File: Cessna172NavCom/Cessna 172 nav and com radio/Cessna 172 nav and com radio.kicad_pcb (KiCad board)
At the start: 2 copper layers, 33 parts, among them J1 Board connector, U1 MAX7219 COM standby, U2 MAX7219 COM standby, U3 MAX7219 COM standby, U4 MAX7219 COM standby

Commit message: 3D model for LED
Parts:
- added C5: 0.1uf, Capacitor_THT:C_Disc_D3.0mm_W2.0mm_P2.50mm, F.Cu at (189.8, 95.3)
- added C6: 0.1uf, Capacitor_THT:C_Disc_D3.0mm_W2.0mm_P2.50mm, F.Cu at (213.0, 52.6)
- added J1: Conn_02x08_Counter_Clockwise, Connector_PinHeader_2.54mm:PinHeader_1x16_P2.54mm_Vertical, F.Cu at (190.5, 53.1)
- added R5: 10k, Resistor_SMD:R_0805_2012Metric_Pad1.15x1.40mm_HandSolder, F.Cu at (195.2, 67.5)
- added R6: 10k, Resistor_SMD:R_0805_2012Metric_Pad1.15x1.40mm_HandSolder, F.Cu at (200.0, 67.5)
- added R7: 10k, Resistor_SMD:R_0805_2012Metric_Pad1.15x1.40mm_HandSolder, F.Cu at (204.7, 67.5)
- added R8: 10k, Resistor_SMD:R_0805_2012Metric_Pad1.15x1.40mm_HandSolder, F.Cu at (209.5, 67.5)
- added SW1: Tuning encoder, Rotary_Encoder:RotaryEncoder_Alps_EC11E-Switch_Vertical_H20mm, F.Cu at (194.9, 55.9)
- LED1, LED10, LED11, LED12, LED13, LED14, LED15, LED16, LED17, LED18, LED19, LED2, LED20, LED3, LED4, LED5, LED6, LED7, LED8, LED9: footprint Display_7Segment:KCSC02-105 -> Cessna 172 nav and com radio:KYX-5101AS
- U1, U2, U3, U4: footprint Package_DIP:DIP-24_W7.62mm -> Package_SO:SSOP-24_3.9x8.7mm_P0.635mm
- moved LED6 37.5 mm to (55.9, 86.4)
- moved LED7 22.8 mm to (94.0, 86.4)
- moved LED8 22.2 mm to (68.6, 86.4)
- moved LED10 14.6 mm to (106.7, 86.4)
- moved LED9 7.07 mm to (81.3, 86.4)

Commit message: 3d model updates
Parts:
- R1, R2, U1, U2: moved to B.Cu
- moved R2 52.3 mm to (59.7, 48.3)
- moved R1 51.9 mm to (58.4, 26.7)
- moved LED3 41.7 mm to (45.7, 26.7)
- moved LED10 39.4 mm to (96.5, 48.3)
- moved LED7 39.4 mm to (83.8, 48.3)
- moved LED6 39.4 mm to (45.7, 48.3)
- moved LED8 39.4 mm to (58.4, 48.3)
- moved LED9 39.4 mm to (71.1, 48.3)
- moved LED4 29.6 mm to (71.1, 26.7)
- moved LED5 27.9 mm to (58.4, 26.7)
- moved LED2 17.8 mm to (83.8, 26.7)
- moved U2 14.2 mm to (71.1, 48.3), turned to 270 degrees
- moved LED1 10.0 mm to (96.5, 26.7)
- moved U1 1.88 mm to (71.1, 26.7), turned to 270 degrees

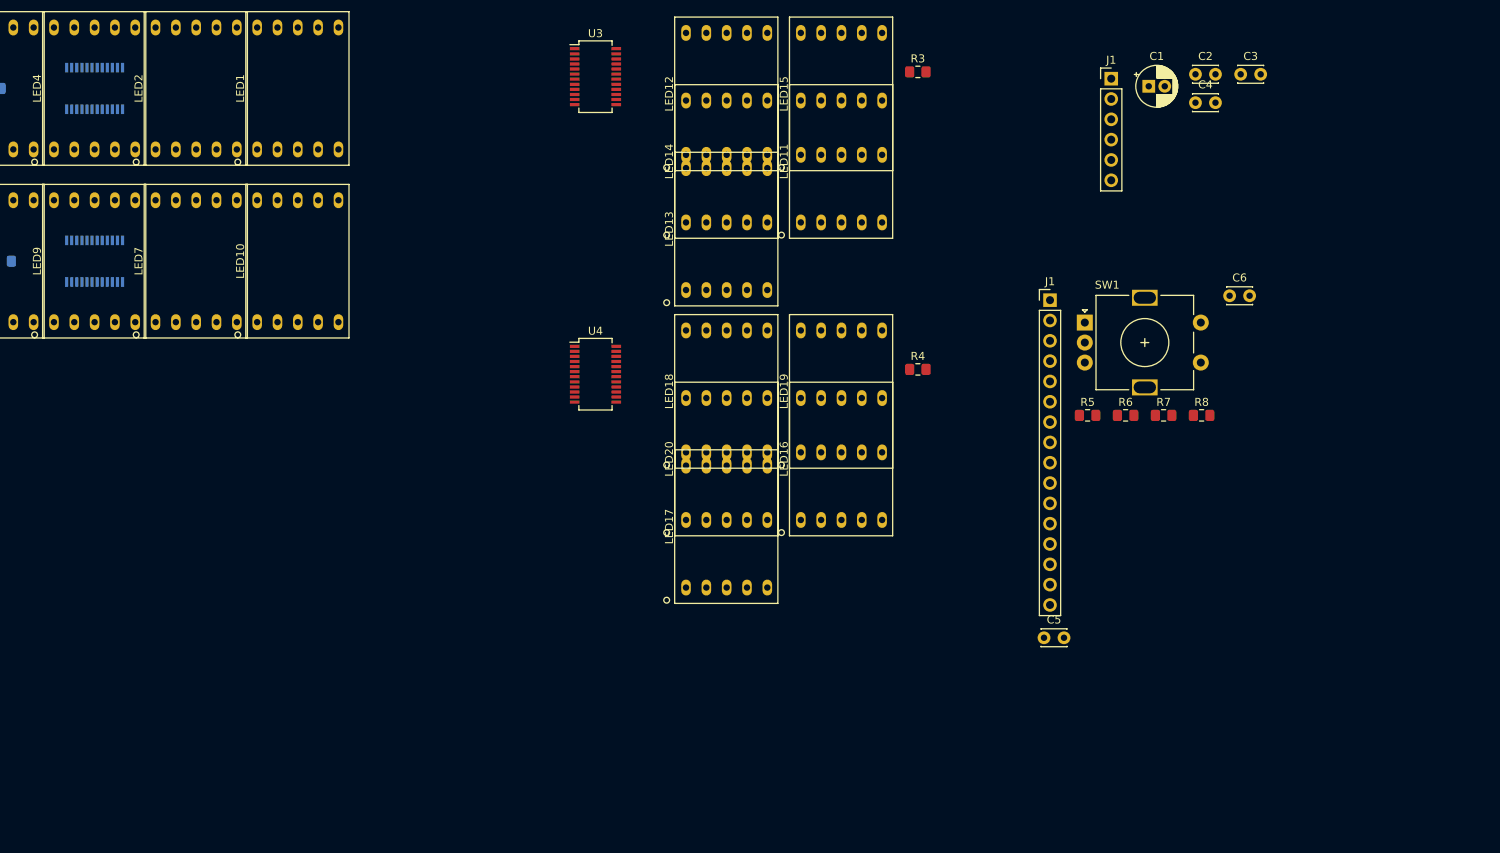
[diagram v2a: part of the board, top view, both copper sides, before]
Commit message: Updated schematic to include remaining items.
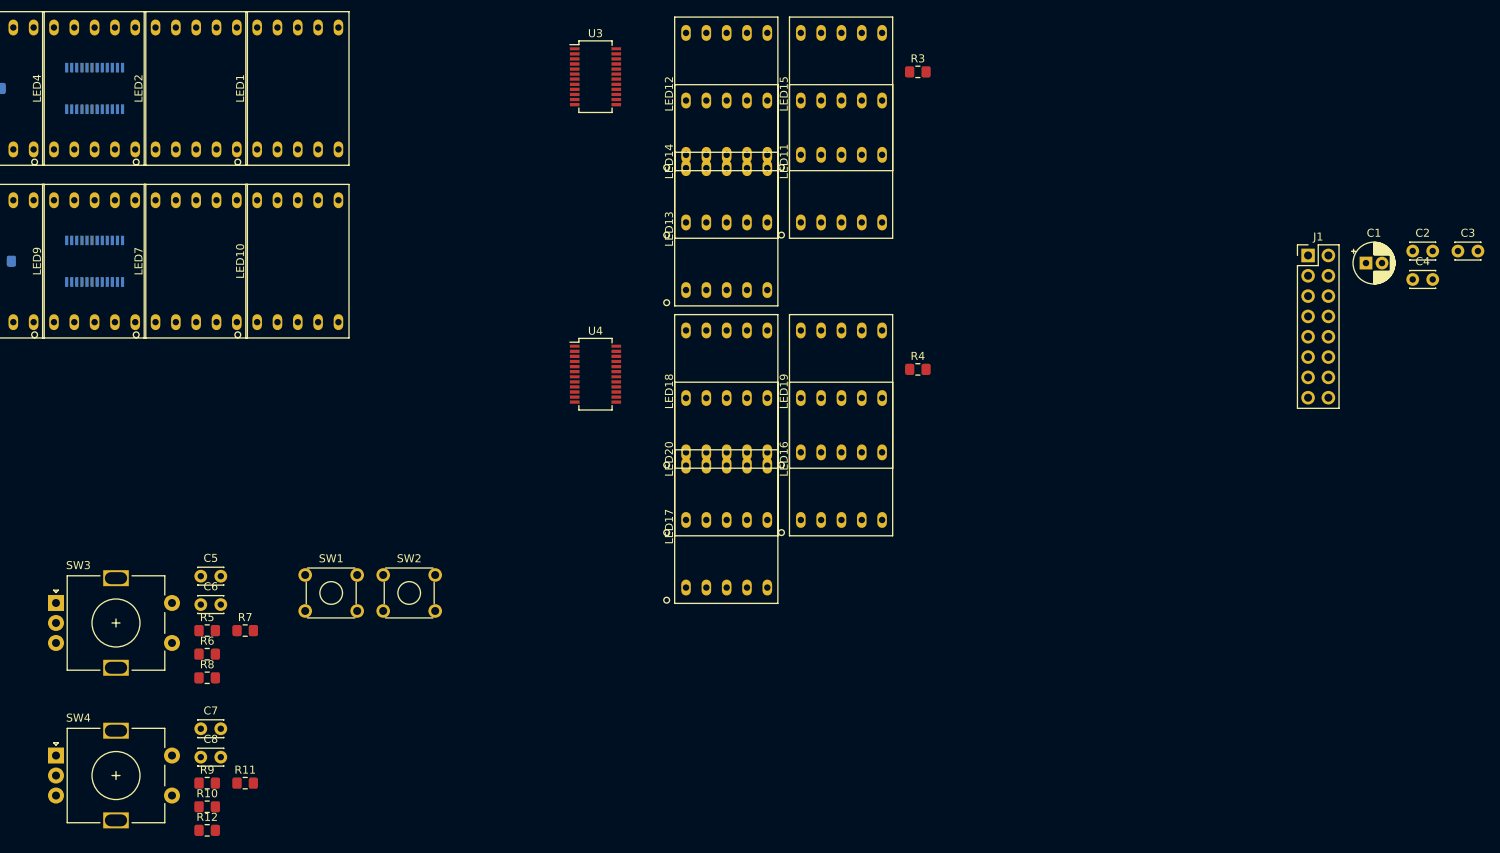
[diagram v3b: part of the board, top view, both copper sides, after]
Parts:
- removed the J1 at (198.2, 25.4)
- removed the J1 at (190.5, 53.1)
- added C7: 0.1uf, Capacitor_THT:C_Disc_D3.0mm_W2.0mm_P2.50mm, F.Cu at (84.4, 106.7)
- added C8: 0.1uf, Capacitor_THT:C_Disc_D3.0mm_W2.0mm_P2.50mm, F.Cu at (84.4, 110.3)
- added J1: Conn_02x08_Counter_Clockwise, Connector_PinHeader_2.54mm:PinHeader_2x08_P2.54mm_Vertical, F.Cu at (222.8, 47.5)
- added R10: 10k, Resistor_SMD:R_0805_2012Metric_Pad1.15x1.40mm_HandSolder, F.Cu at (85.2, 116.5)
- added R11: 10k, Resistor_SMD:R_0805_2012Metric_Pad1.15x1.40mm_HandSolder, F.Cu at (89.9, 113.5)
- added R12: 10k, Resistor_SMD:R_0805_2012Metric_Pad1.15x1.40mm_HandSolder, F.Cu at (85.2, 119.4)
- added R9: 10k, Resistor_SMD:R_0805_2012Metric_Pad1.15x1.40mm_HandSolder, F.Cu at (85.2, 113.5)
- added SW2: NAV transfer switch, Button_Switch_THT:SW_TH_Tactile_Omron_B3F-10xx, F.Cu at (107.2, 87.5)
- added SW3: Tuning encoder, Rotary_Encoder:RotaryEncoder_Alps_EC11E-Switch_Vertical_H20mm, F.Cu at (66.3, 91.0)
- added SW4: Tuning encoder, Rotary_Encoder:RotaryEncoder_Alps_EC11E-Switch_Vertical_H20mm, F.Cu at (66.3, 110.1)
- SW1: value Tuning encoder -> COMM transfer switch; footprint Rotary_Encoder:RotaryEncoder_Alps_EC11E-Switch_Vertical_H20mm -> Button_Switch_THT:SW_TH_Tactile_Omron_B3F-10xx
- moved C6 134.3 mm to (84.4, 91.2)
- moved R8 128.6 mm to (85.2, 100.3)
- moved R6 118.6 mm to (85.2, 97.4)
- moved R7 117.9 mm to (89.9, 94.4)
- moved R5 113.3 mm to (85.2, 94.4)
- moved C5 105.7 mm to (84.4, 87.6)
- moved SW1 102.4 mm to (97.4, 87.5)
- moved C1 35.0 mm to (230.0, 48.5)
- moved C3 35.0 mm to (241.5, 47.0)
- moved C2 35.0 mm to (235.9, 47.0)
- moved C4 35.0 mm to (235.9, 50.5)
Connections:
- R5 pad 1: R_RIGHT -> Net-(C5-Pad2)
- R5 pad 2: Net-(C5-Pad2) -> +5V
- R6 pad 1: Net-(C5-Pad2) -> Net-(C6-Pad1)
- R7 pad 1: Net-(C6-Pad1) -> COMM_RIGHT
- R7 pad 2: +5V -> Net-(C5-Pad2)
- R8 pad 2: R_LEFT -> COMM_LEFT

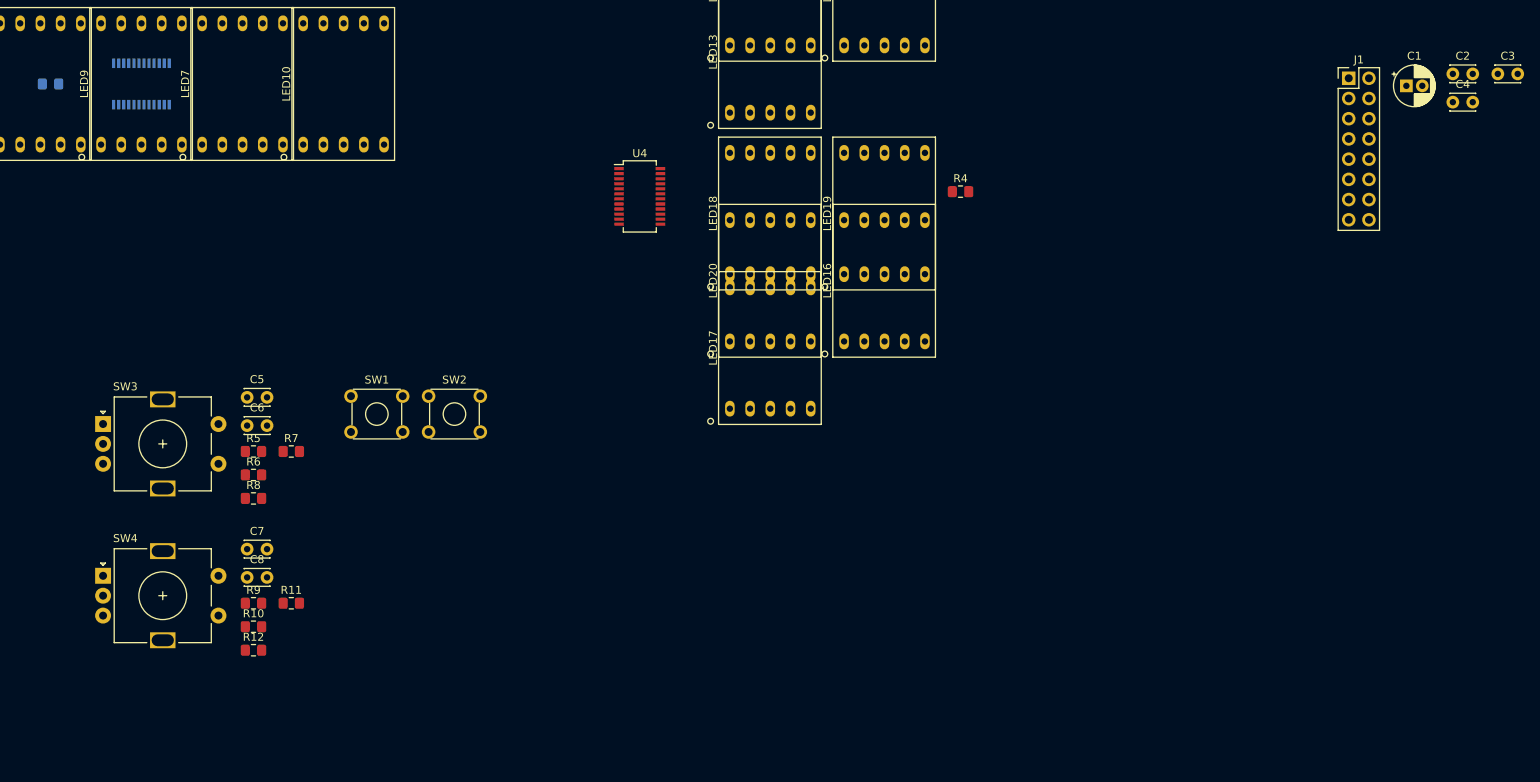
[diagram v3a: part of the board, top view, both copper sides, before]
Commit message: Proper LED buttons and switches
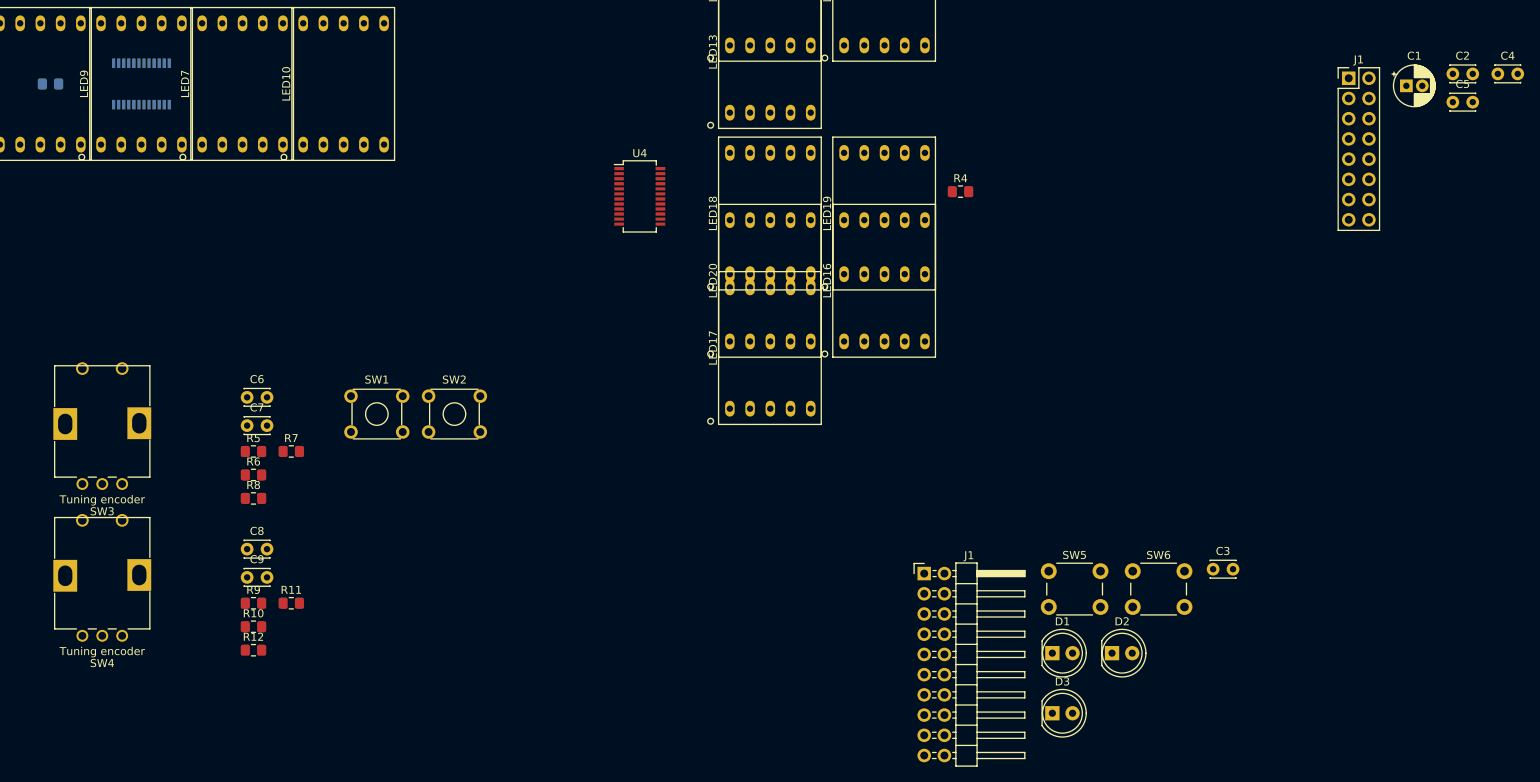
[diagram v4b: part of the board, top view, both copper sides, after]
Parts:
- added C3: 0.1uF, Capacitor_THT:C_Disc_D3.0mm_W2.0mm_P2.50mm, F.Cu at (205.8, 109.2)
- added D1: CHAN LED, LED_THT:LED_D5.0mm, F.Cu at (185.6, 119.8)
- added D2: IDENT LED, LED_THT:LED_D5.0mm, F.Cu at (193.1, 119.8)
- added D3: MODE LED, LED_THT:LED_D5.0mm, F.Cu at (185.6, 127.3)
- added J1: Conn_02x10_Counter_Clockwise, Connector_PinHeader_2.54mm:PinHeader_2x10_P2.54mm_Horizontal, F.Cu at (169.5, 109.8)
- added SW5: TEST, Button_Switch_THT:SW_PUSH_6mm, F.Cu at (185.1, 109.5)
- added SW6: IDENT, Button_Switch_THT:SW_PUSH_6mm, F.Cu at (195.7, 109.5)
- SW3, SW4: footprint Rotary_Encoder:RotaryEncoder_Alps_EC11E-Switch_Vertical_H20mm -> Cessna 172 nav and com radio:EN11-HSM1BF20
- renumbered C3 to C4, C4 to C5, C5 to C6, C6 to C7, C7 to C8, C8 to C9
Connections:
- C6 pad 2: Net-(C5-Pad2) -> Net-(C6-Pad2)
- C7 pad 1: Net-(C6-Pad1) -> Net-(C7-Pad1)
- C8 pad 2: Net-(C7-Pad2) -> Net-(C8-Pad2)
- C9 pad 1: Net-(C8-Pad1) -> Net-(C9-Pad1)
- R10 pad 1: Net-(C8-Pad1) -> Net-(C9-Pad1)
- R11 pad 2: Net-(C7-Pad2) -> Net-(C8-Pad2)
- R12 pad 1: Net-(C8-Pad1) -> Net-(C9-Pad1)
- R5 pad 1: Net-(C5-Pad2) -> Net-(C6-Pad2)
- R6 pad 1: Net-(C6-Pad1) -> Net-(C7-Pad1)
- R7 pad 2: Net-(C5-Pad2) -> Net-(C6-Pad2)
- R8 pad 1: Net-(C6-Pad1) -> Net-(C7-Pad1)
- R9 pad 1: Net-(C7-Pad2) -> Net-(C8-Pad2)

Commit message: Tactile switch
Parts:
- removed C1: 10uF, Capacitor_THT:CP_Radial_D5.0mm_P2.00mm
- removed C2, C3, C4, C5: 0.1uF, Capacitor_THT:C_Disc_D3.0mm_W2.0mm_P2.50mm
- removed D1: CHAN LED, LED_THT:LED_D5.0mm
- removed D2: IDENT LED, LED_THT:LED_D5.0mm
- removed D3: MODE LED, LED_THT:LED_D5.0mm
- removed the J1 at (222.8, 47.5)
- removed the J1 at (169.5, 109.8)
- removed R1, R2, R3, R4: 27k, Resistor_SMD:R_0805_2012Metric_Pad1.15x1.40mm_HandSolder
- added J1: Conn_02x12_Odd_Even, Connector_PinHeader_2.54mm:PinHeader_2x12_P2.54mm_Vertical, B.Cu at (102.9, 87.6)
- added RV1: 100k, Potentiometer_THT:Potentiometer_Piher_PT-10-V10_Vertical_Hole, B.Cu at (121.9, 34.3)
- added SW1: COMM toggle, Cessna 172 nav and com radio:B3W-9000-xxx, F.Cu at (127.0, 55.9)
- added SW2: NAV toggle, Cessna 172 nav and com radio:B3W-9000-xxx, F.Cu at (275.6, 55.9)
- C6, C7, C8, C9: footprint Capacitor_THT:C_Disc_D3.0mm_W2.0mm_P2.50mm -> Capacitor_SMD:C_0805_2012Metric_Pad1.15x1.40mm_HandSolder
- SW5: value TEST -> Test switch; footprint Button_Switch_THT:SW_PUSH_6mm -> Cessna 172 nav and com radio:B3W-9000-xxx
- SW6: value IDENT -> Ident switch; footprint Button_Switch_THT:SW_PUSH_6mm -> Cessna 172 nav and com radio:B3W-9000-xxx
- U3, U4: moved to B.Cu
- moved SW4 270.7 mm to (335.3, 80.0)
- moved LED17 193.2 mm to (341.6, 55.9)
- moved U4 182.6 mm to (316.2, 55.9), turned to 270 degrees
- moved LED20 179.6 mm to (328.9, 55.9)
- moved LED16 152.7 mm to (316.2, 55.9)
- moved LED18 141.0 mm to (290.8, 55.9)
- moved LED19 139.3 mm to (303.5, 55.9)
- moved SW3 120.8 mm to (186.7, 81.3)
- moved LED13 110.8 mm to (260.4, 55.9)
- moved U3 105.8 mm to (234.9, 55.9), turned to 270 degrees
- moved LED6 96.8 mm to (142.2, 55.9)
- moved LED7 96.8 mm to (180.3, 55.9)
- moved LED10 96.8 mm to (193.0, 55.9)
- moved LED8 96.8 mm to (154.9, 55.9)
- moved LED9 96.8 mm to (167.6, 55.9)
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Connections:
- SW5 pad 1: GND -> Net-(SW5-Pad1)
- SW5 pad 2: TEST_SW -> Net-(SW5-Pad2)
- SW6 pad 1: GND -> Net-(SW6-Pad1)
- SW6 pad 2: IDENT_SW -> Net-(SW6-Pad2)
- U1 pad 18: Net-(R1-Pad1) -> ISET
- U1 pad 19: GND -> +5V
- U2 pad 18: Net-(R2-Pad1) -> ISET
- U2 pad 19: GND -> +5V
- U3 pad 18: Net-(R3-Pad1) -> ISET
- U3 pad 19: GND -> +5V
- U4 pad 18: Net-(R4-Pad1) -> ISET
- U4 pad 19: GND -> +5V
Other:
- board outline added: 330.2 x 76.2 mm
